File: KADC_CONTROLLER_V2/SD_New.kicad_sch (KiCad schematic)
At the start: 28 parts, among them IC2 NVT4858HKZ, J8 1040310811, U22 TPS22913BYZVT, U23 NX3P1108UKZ, U24 74AUP1G04GW-Q100, U25 NX3P1108UKZ, U6 74AUP1G04GW-Q100

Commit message: Now updates kadc, forgot to save
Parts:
- removed C60: 0.1u, Capacitor_SMD:C_0603_1608Metric, symbol Device:C_Small
- removed R58, R66, R68: 0R, Resistor_SMD:R_0603_1608Metric, symbol Device:R_Small_US
- removed U6: 74AUP1G04GW-Q100, Package_TO_SOT_SMD:SOT-353_SC-70-5, symbol 74AUP1G04GW:74AUP1G04GW-Q100
- added R125: 10k, Resistor_SMD:R_0603_1608Metric, symbol Device:R_Small_US
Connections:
- net 1V8_Banks: now also R123.1, R125.2
- net 3V3_IO: no longer R123.1
- net SD_SEL: now also U23.B2 (EN), U24.2 (A), R125.1
- no-connect marks 2 -> 1

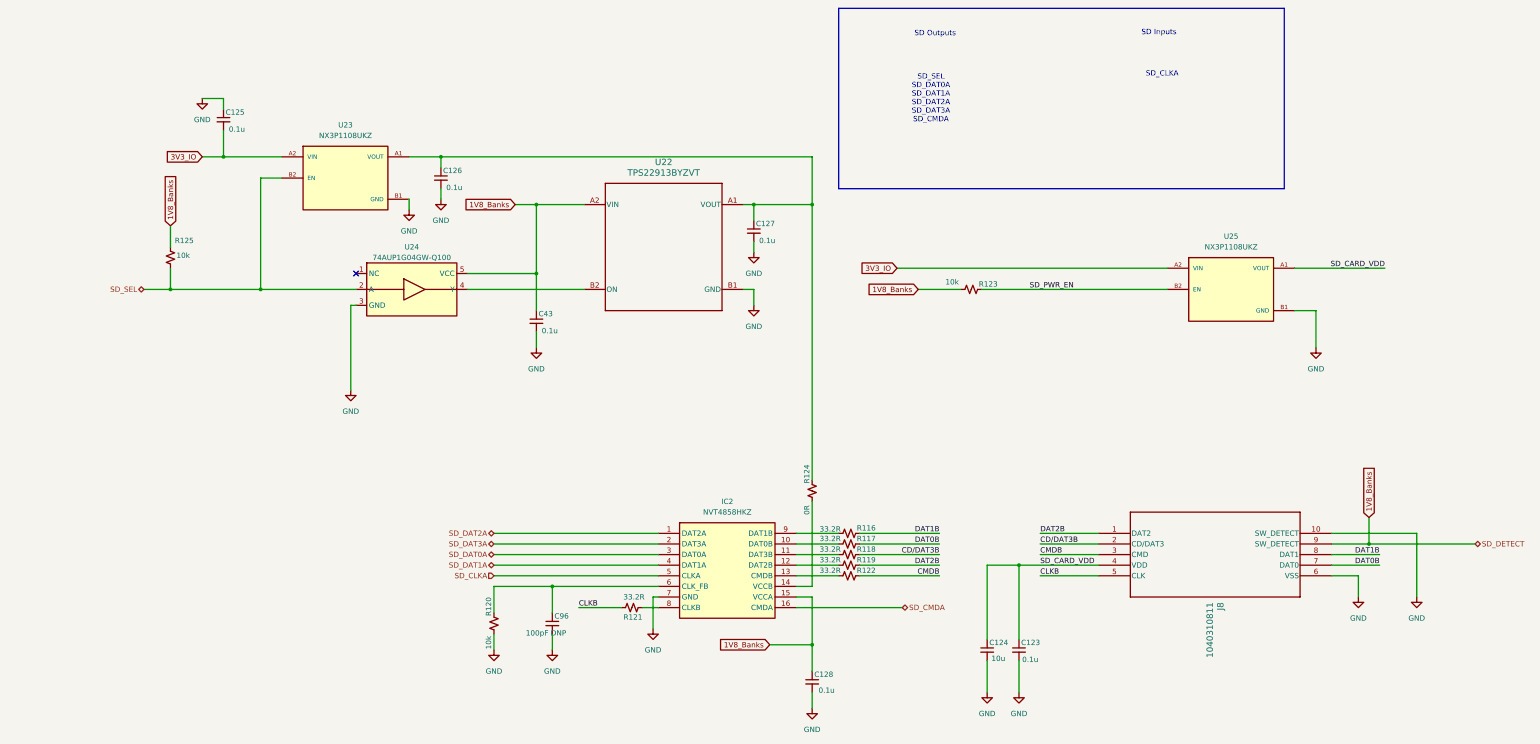
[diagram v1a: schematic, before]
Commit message: Many Updates
Starting new power sequence and implementing KR260 PS circuitry.
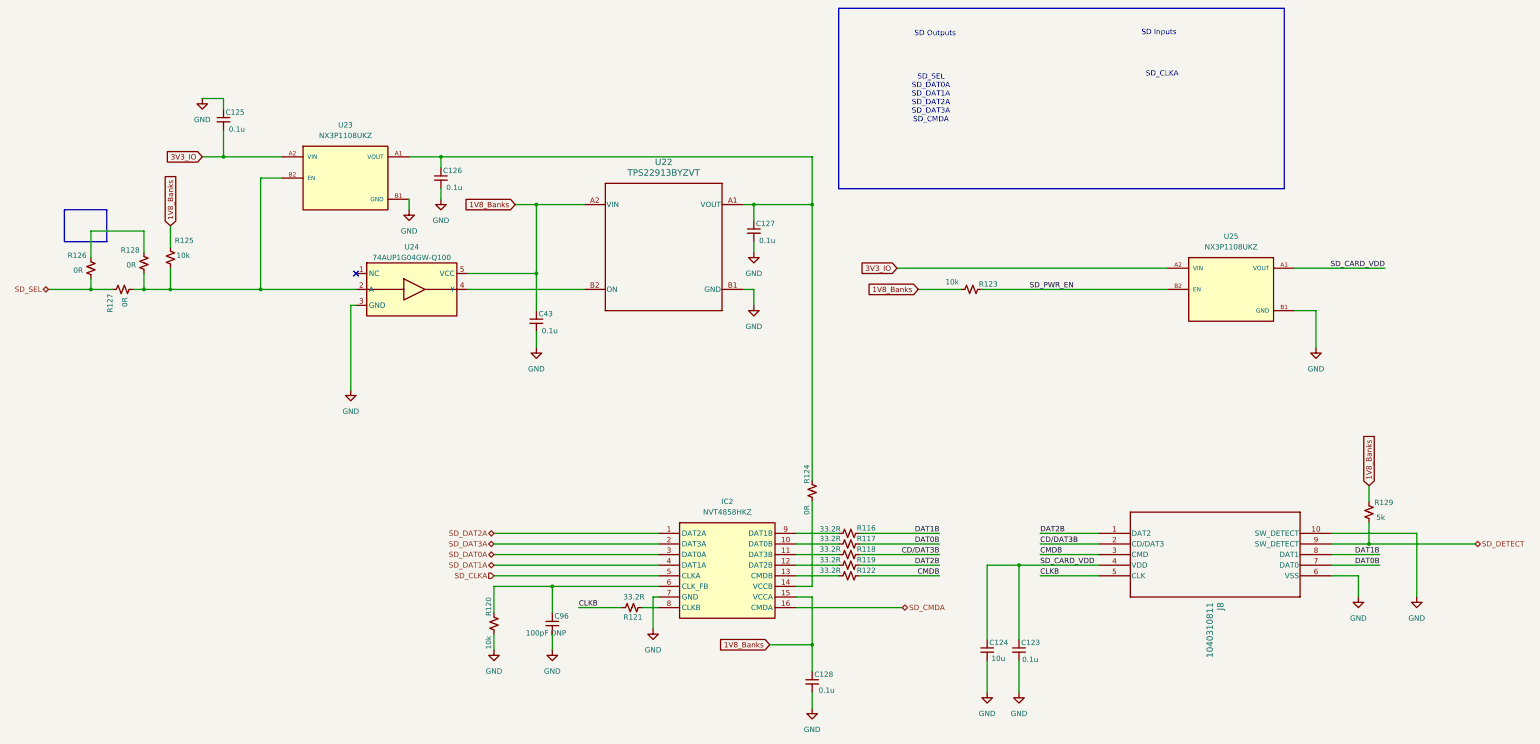
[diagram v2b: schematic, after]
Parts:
- added R126, R127, R128: 0R, Resistor_SMD:R_0603_1608Metric, symbol Device:R_Small_US
- added R129: 5k, Resistor_SMD:R_0603_1608Metric, symbol Device:R_Small_US
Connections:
- net 1V8_Banks: now also R129.2; no longer J8.9 (SW_DETECT)
- net SD_SEL: now also R126.2, R127.1; no longer R125.1, U23.B2 (EN), U24.2 (A)
- new net: R125.1, R127.2, R128.2, U23.B2 (EN), U24.2 (A)
- new net: R126.1, R128.1
- new net SD_DETECT: J8.9 (SW_DETECT), R129.1
